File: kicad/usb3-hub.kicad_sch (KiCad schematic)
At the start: 12 parts, among them J101 DISPLAY, J102 USB3_B_Micro, J103 Barrel_Jack_Switch

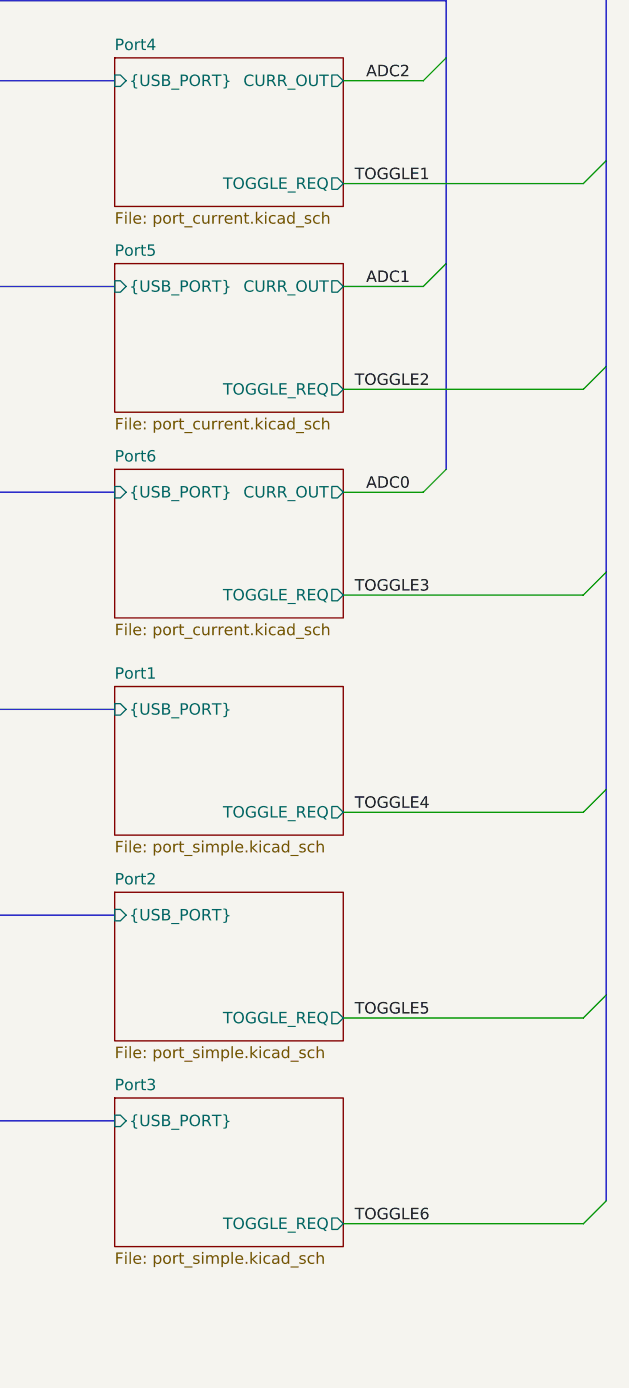
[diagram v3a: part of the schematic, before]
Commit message: Some more routing
rearranged the LED's
Exchanged the testpoints with a 1x5 connector.
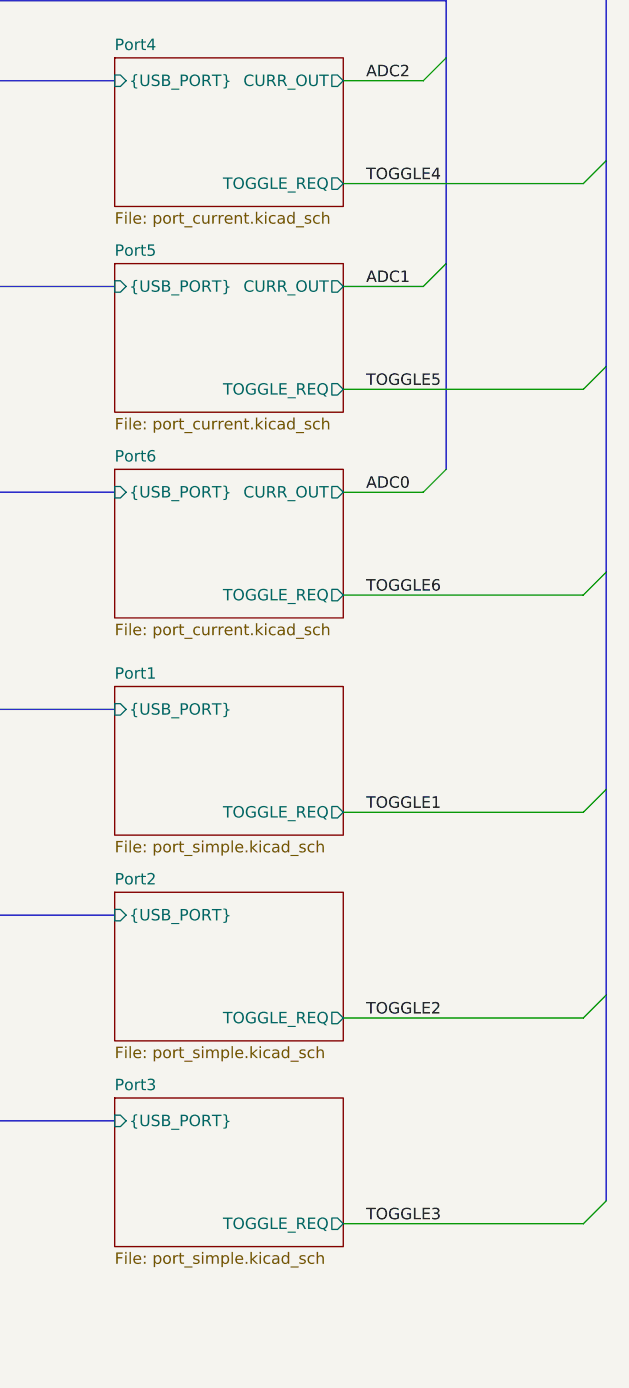
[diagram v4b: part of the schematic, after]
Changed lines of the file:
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@@
 	)
 	(label "TOGGLE6"
-		(at 243.84 157.48 0)
+		(at 245.11 87.63 0)
 		(fields_autoplaced yes)
 		(effects
@@
 	)
 	(label "TOGGLE5"
-		(at 243.84 134.62 0)
+		(at 245.11 64.77 0)
 		(fields_autoplaced yes)
 		(effects
@@
 	)
 	(label "TOGGLE1"
-		(at 243.84 41.91 0)
+		(at 245.11 111.76 0)
 		(fields_autoplaced yes)
 		(effects
@@
 	)
 	(label "TOGGLE3"
-		(at 243.84 87.63 0)
+		(at 245.11 157.48 0)
 		(fields_autoplaced yes)
 		(effects
@@
 	)
 	(label "TOGGLE2"
-		(at 243.84 64.77 0)
+		(at 245.11 134.62 0)
 		(fields_autoplaced yes)
 		(effects
@@
 	)
 	(label "TOGGLE4"
-		(at 243.84 111.76 0)
-		(fields_autoplaced yes)
-		(effects
+		(at 245.11 41.91 0)
+		(fields_autoplaced yes)
+		(effects

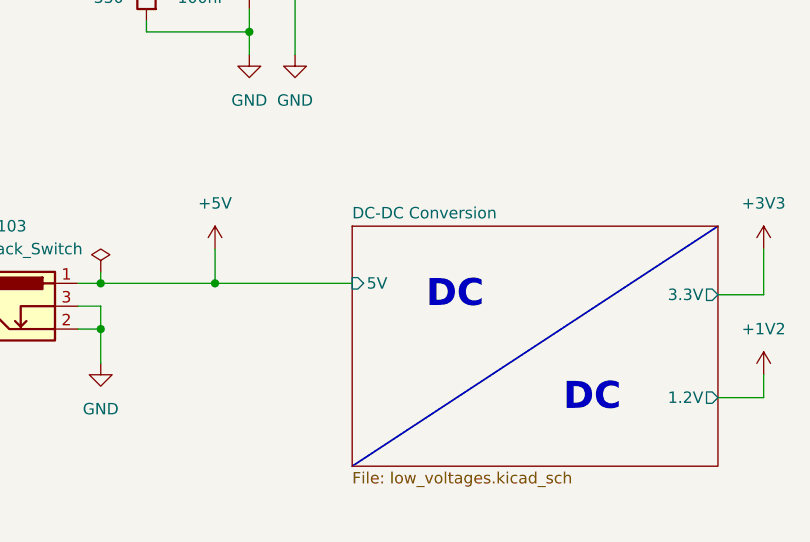
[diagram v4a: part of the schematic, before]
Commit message: Replace 1.2V LDO with switching regulator
It just feels more reliable.
Also added 0R resistors between switch and alert signal. My hope is
that I can tell the switch to diable the port by pulling the
overcurrent low.
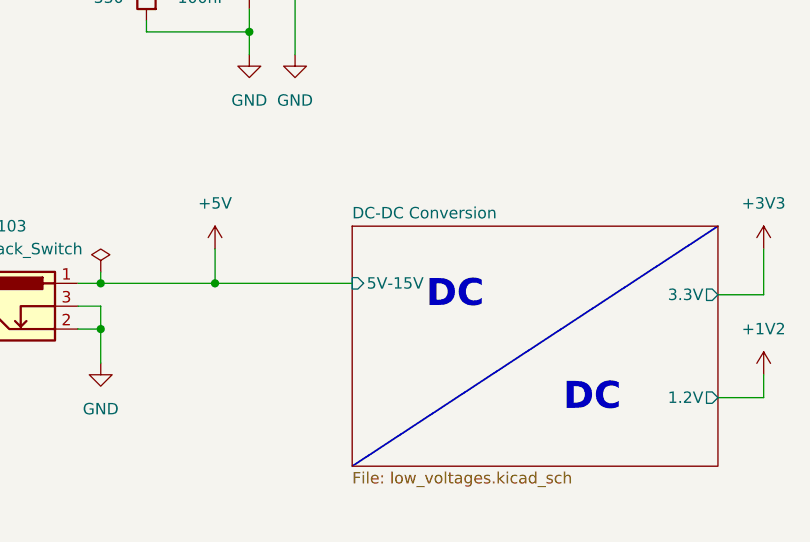
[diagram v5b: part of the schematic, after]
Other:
- sheet DC-DC Conversion ports: added 5V-15V; removed 5V
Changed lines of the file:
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@@
-			)
-		)
-		(pin "5V" input
-			(at 93.98 167.64 180)
-			(effects
-				(font
-					(size 1.27 1.27)
-				)
-				(justify left)
 			)
 		)
@@
 			)
 		)
+		(pin "5V-15V" input
+			(at 93.98 167.64 180)
+			(effects
+				(font
+					(size 1.27 1.27)
+				)
+				(justify left)
+			)
+		)
